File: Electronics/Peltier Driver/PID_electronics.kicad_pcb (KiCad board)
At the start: 2 copper layers, 76.2 x 43.3 mm, 24 parts, among them J1 Conn_01x05, J2 Conn_01x03, Q3 2N7000, U1 LF412

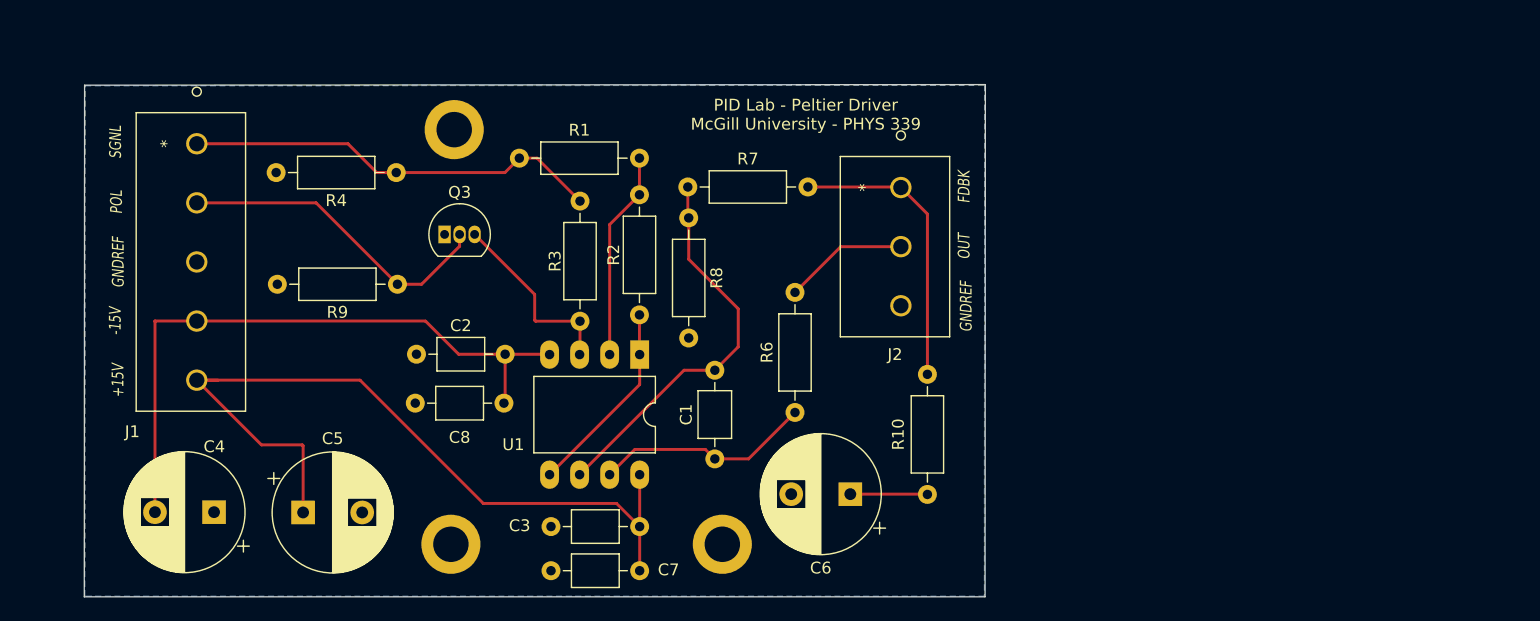
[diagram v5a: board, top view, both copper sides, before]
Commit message: Replaced Opamp footprint with socket footprint
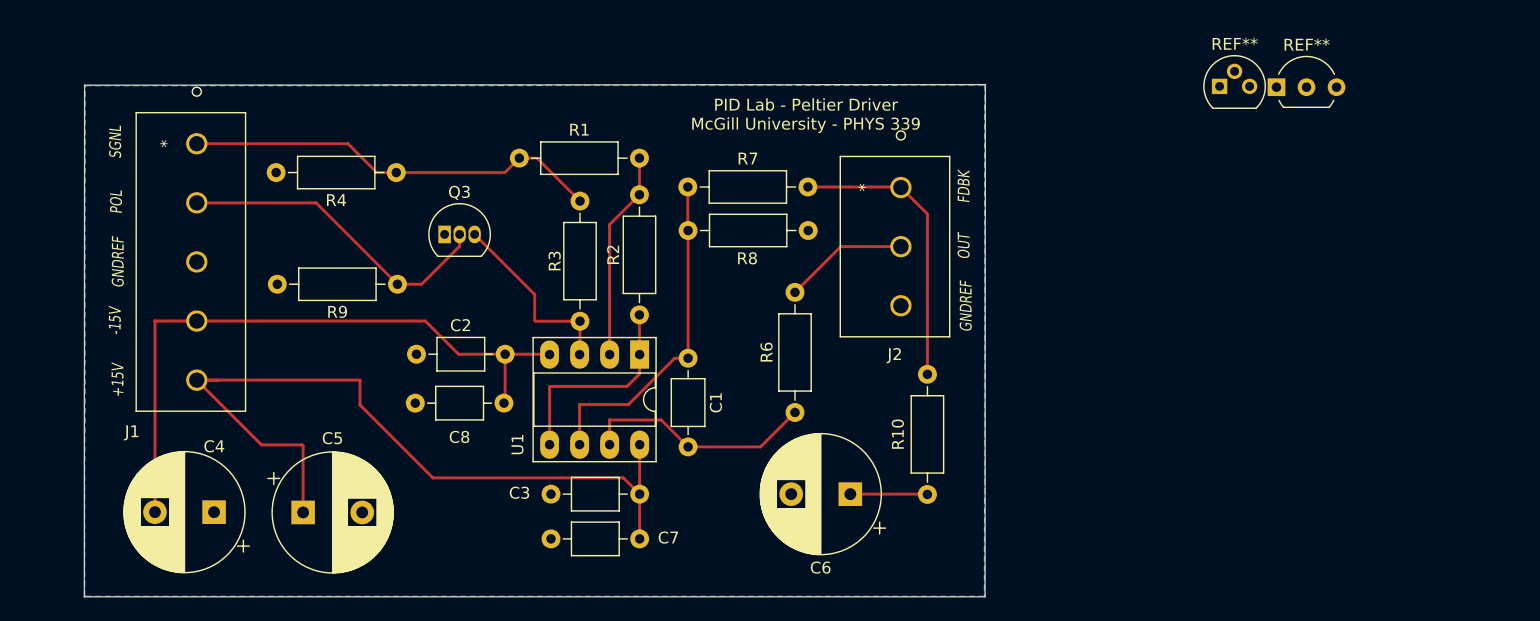
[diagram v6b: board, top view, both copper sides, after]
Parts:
- removed ? (x3): , 
- added REF**: TO-92L_Inline_Wide, Package_TO_SOT_THT:TO-92L_Inline_Wide, F.Cu at (184.7, 71.4)
- added REF**: TO-92, Package_TO_SOT_THT:TO-92, F.Cu at (179.9, 71.3)
- U1: footprint Package_DIP:DIP-8_W10.16mm_LongPads -> Package_DIP:DIP-8_W7.62mm_Socket_LongPads
- moved C3 2.74 mm to (130.8, 105.8)
- moved C7 2.69 mm to (130.8, 109.6)
- moved C1 2.48 mm to (134.9, 101.8)
- moved R8 1.07 mm to (134.9, 83.5), turned to 0 degrees
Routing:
- net Net-(C1-Pad2): track 33.2 -> 28.7 mm
- net Net-(C1-Pad1): track 18.5 -> 19.9 mm
- net Net-(R2-Pad2): track 16.7 -> 18.0 mm

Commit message: Added test points, changed 2n7000 T0-92 footprint
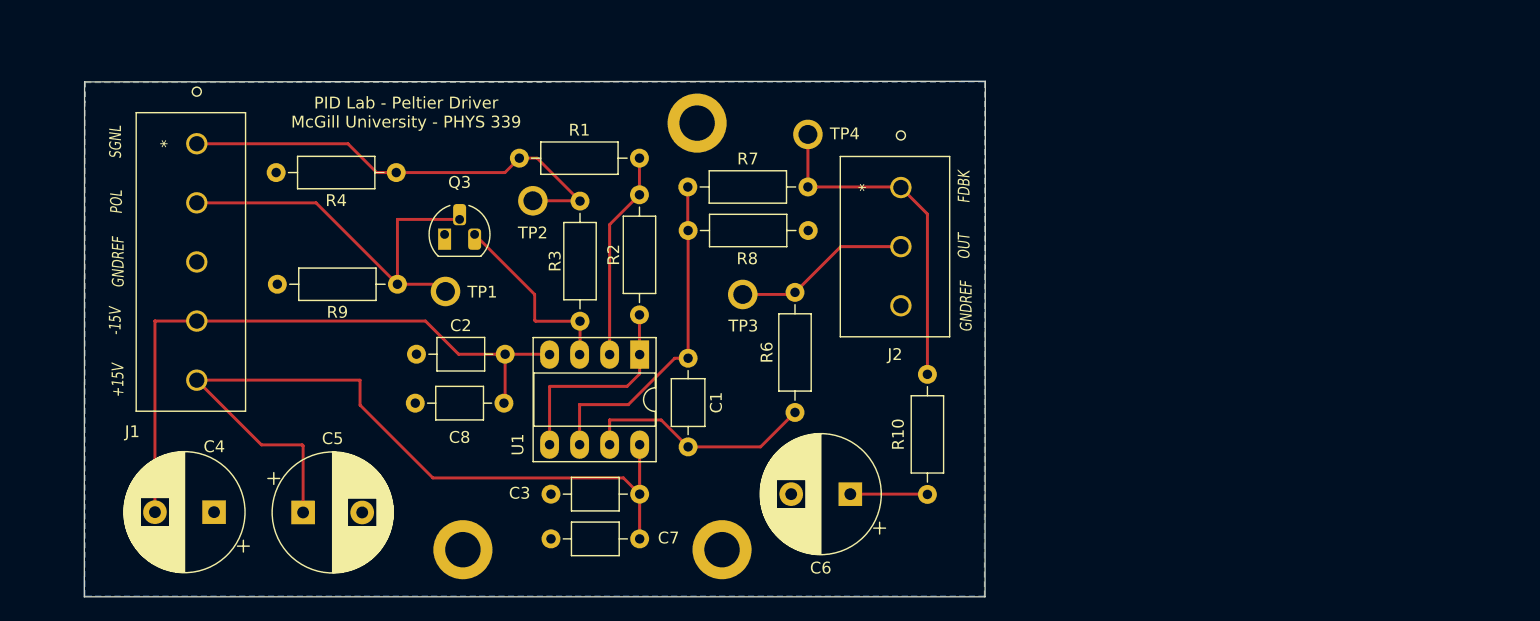
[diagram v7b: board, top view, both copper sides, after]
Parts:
- removed the REF** at (184.7, 71.4)
- removed the REF** at (179.9, 71.3)
- added REF**: TP4, KiCAD_footprints:Test_point, F.Cu at (145.0, 83.0)
- added REF**: mounting hole, KiCAD_footprints:mounting hole, F.Cu at (137.8, 115.4)
- added REF**: mounting hole, KiCAD_footprints:mounting hole, F.Cu at (115.8, 115.6)
- added REF**: TP2, KiCAD_footprints:Test_point, F.Cu at (121.8, 88.6)
- added REF**: TP1, KiCAD_footprints:Test_point, F.Cu at (114.4, 96.3)
- added REF**: mounting hole, KiCAD_footprints:mounting hole, F.Cu at (135.7, 79.5)
- added REF**: TP3, KiCAD_footprints:Test_point, F.Cu at (139.5, 96.5)
- Q3: footprint Package_TO_SOT_THT:TO-92_Inline -> Package_TO_SOT_THT:TO-92_HandSolder
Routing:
- net Net-(Q3-Pad2): track 27.4 -> 34.9 mm
- net Net-(J2-Pad2): track 10.8 -> 15.3 mm
- net Net-(J2-Pad1): track 24.6 -> 29.1 mm
- net Net-(R1-Pad1): track 35.6 -> 39.4 mm
- net +15V: track 69.4 -> 67.6 mm
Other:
- board size 76.2 x 43.3 mm -> 76.2 x 43.6 mm
- board text added: "Remember the Cant"

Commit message: Layout optimization, mounting hole addition
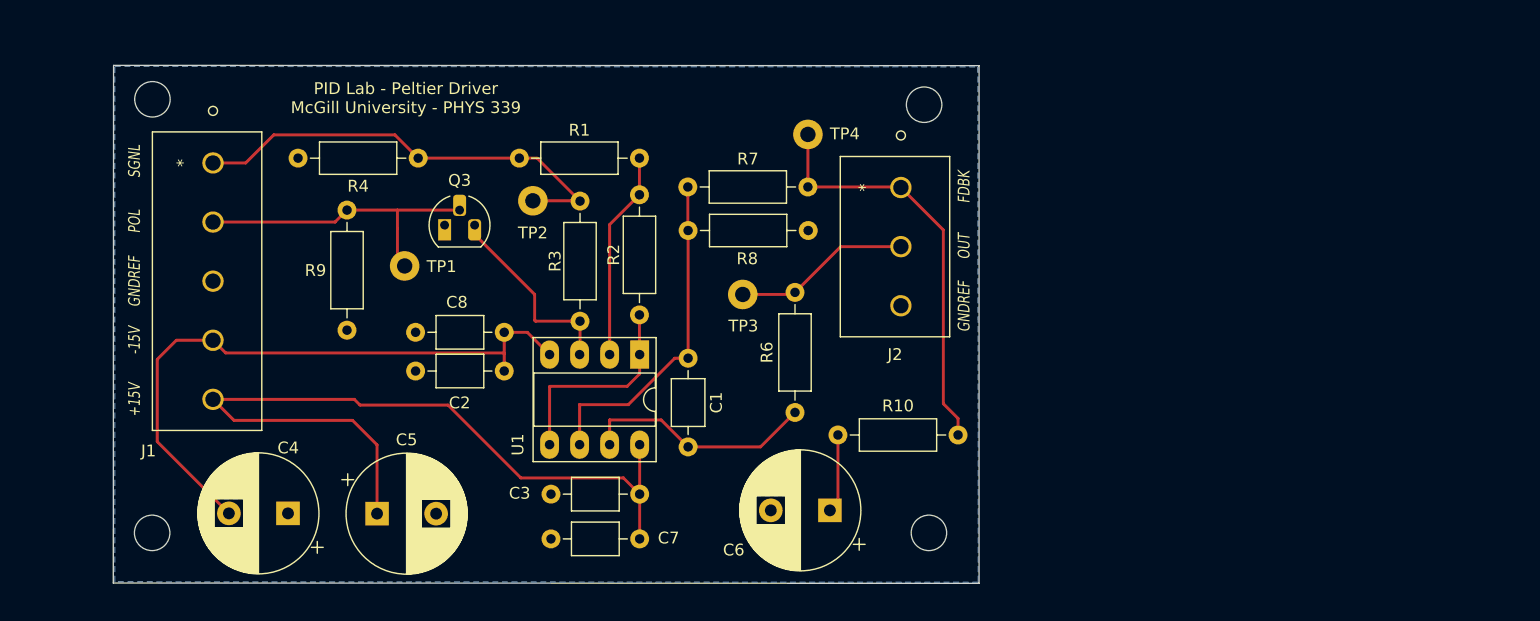
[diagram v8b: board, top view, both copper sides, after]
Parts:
- removed the REF** at (137.8, 115.4)
- removed the REF** at (115.8, 115.6)
- added REF**: mounting hole, KiCAD_footprints:mounting hole, F.Cu at (89.6, 77.5)
- added REF**: mounting hole, KiCAD_footprints:mounting hole, F.Cu at (89.6, 114.1)
- added REF**: mounting hole, KiCAD_footprints:mounting hole, F.Cu at (155.3, 114.1)
- moved REF** 19.3 mm to (154.9, 77.9)
- moved R9 7.59 mm to (106.0, 81.8), turned to -90 degrees
- moved C4 6.25 mm to (101.1, 107.4)
- moved C5 6.25 mm to (108.6, 107.4)
- moved C8 5.99 mm to (111.8, 92.1)
- moved R10 5.75 mm to (157.7, 100.8), turned to 180 degrees
- moved REF** 4.07 mm to (110.9, 94.1)
- moved R4 2.22 mm to (112.1, 77.4)
- moved C6 2.21 mm to (146.9, 107.2)
- moved J1 2.13 mm to (94.7, 77.8)
- moved C2 1.42 mm to (111.8, 95.4)
- moved Q3 0.79 mm to (114.3, 83.0)
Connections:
- REF** pad : GNDREF -> (no net)
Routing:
- net Net-(Q3-Pad2): track 34.9 -> 26.3 mm
- net Net-(J2-Pad1): track 29.1 -> 35.3 mm
- net Net-(R1-Pad1): track 39.4 -> 38.4 mm
- net +15V: track 67.6 -> 68.7 mm
- net -15V: track 54.9 -> 53.9 mm
- net Net-(Q3-Pad3): track 16.1 -> 16.9 mm
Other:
- board size 76.2 x 43.6 mm -> 73.2 x 43.8 mm
